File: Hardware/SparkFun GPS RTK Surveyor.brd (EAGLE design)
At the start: 68.2 x 110.1 mm, 194 parts, among them J13 Internal, J16 microSD, J17 Qwiic Right Angle, J3 USB Female Type C Connector, J4 External, J5 USB Female Type C Connector, Q1 SIL2308-TP, Q10 20V/0.2A/8MHz/1.2Ω/1Vth, Q2 MBT3904DW1T1, Q3 20V/0.2A/8MHz/1.2Ω/1Vth, Q4 20V/0.2A/8MHz/1.2Ω/1Vth, Q7 20V/0.2A/8MHz/1.2Ω/1Vth, Q9 20V/0.2A/8MHz/1.2Ω/1Vth, U1 74HC4052D, U10 MCP73833, U13 9DoF IMU, U14 1.8V/100mA, U2 AP2112K-3.3, U3 U-BLOX_ZED-F9P, U4 ADP160, U5 ESP-WROOM-32NARROW, U6 CH340C, U7 MAX17048

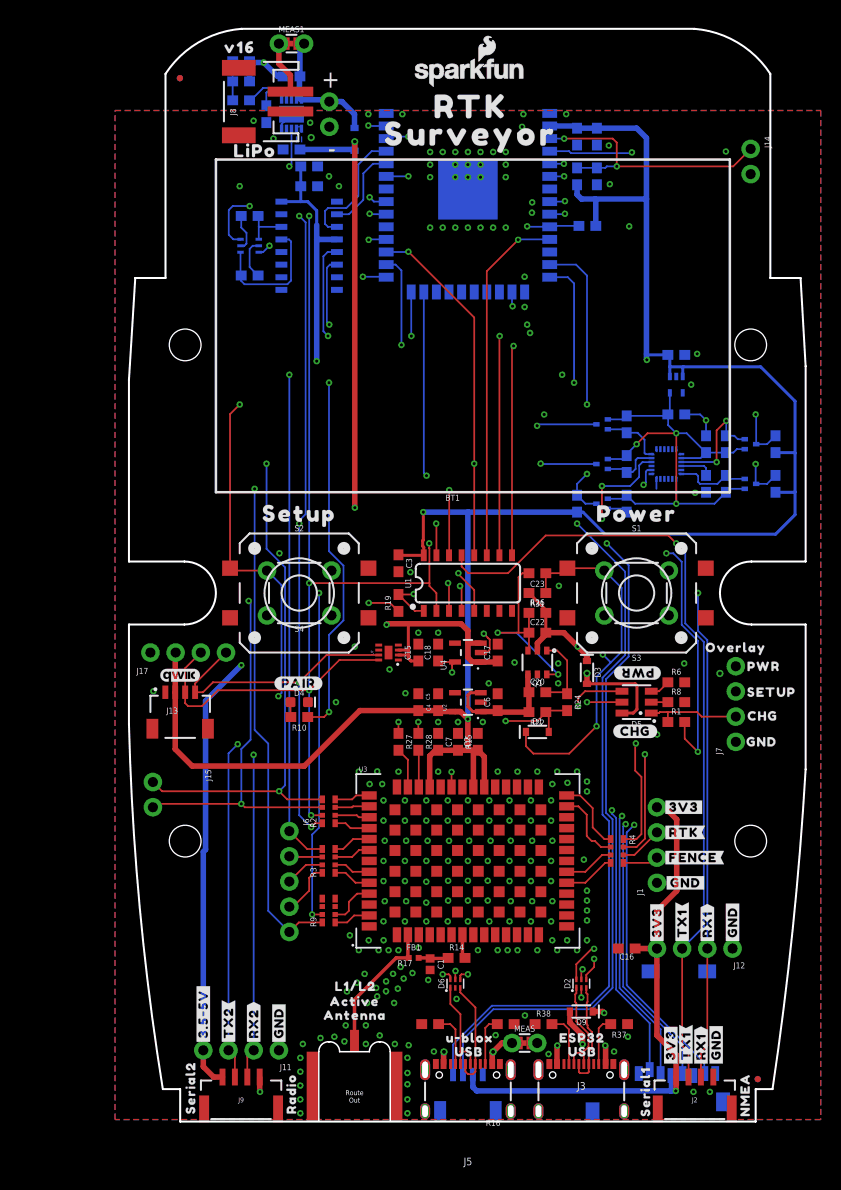
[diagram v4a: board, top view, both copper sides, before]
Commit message: Revert hardware files back to v15
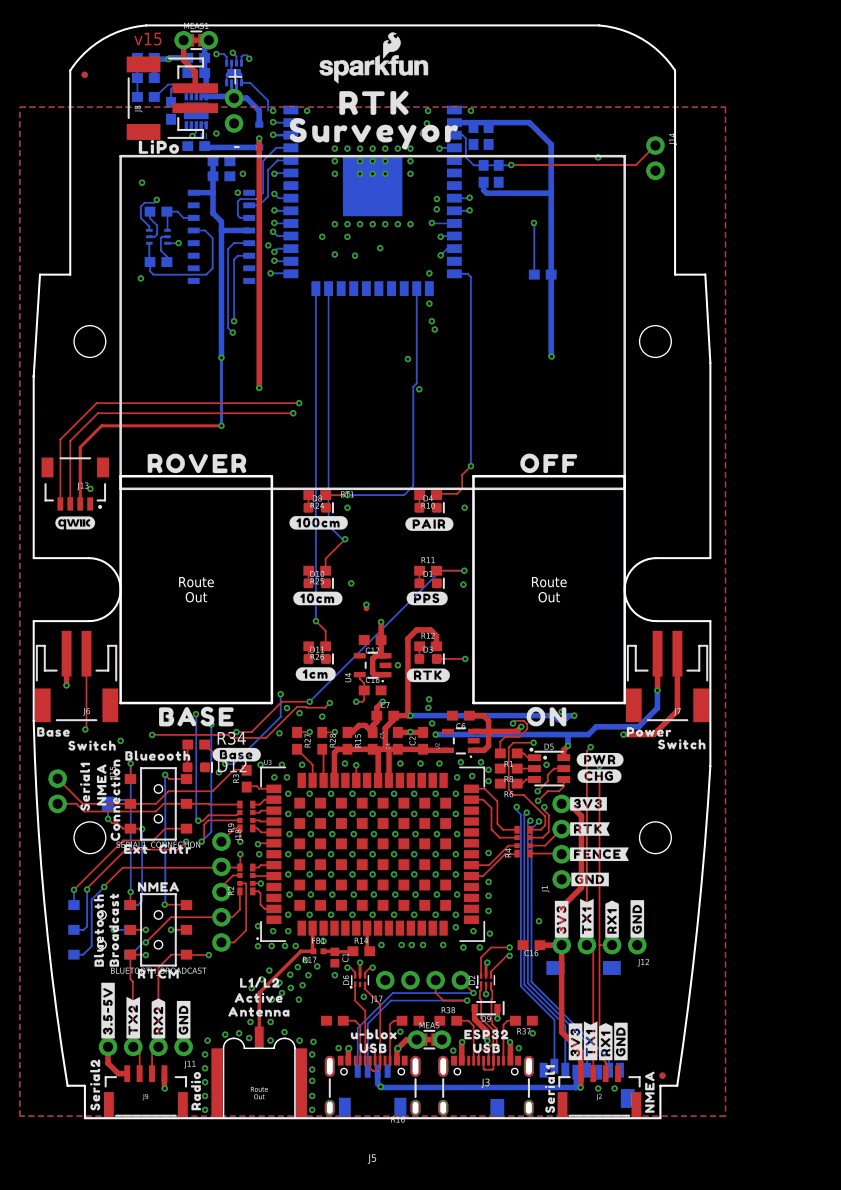
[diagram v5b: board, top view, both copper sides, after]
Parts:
- removed C20: 10uF, SparkFun-Capacitors:0603
- removed C22, C23, C3, C51, C52: 0.1uF, SparkFun-Capacitors:0603
- removed C53, C54: 1.0uF, SparkFun-Capacitors:0603
- removed Q1: SIL2308-TP, SparkFun-DiscreteSemi:SOT26
- removed Q10, Q3, Q4, Q7, Q9: 20V/0.2A/8MHz/1.2Ω/1Vth, SparkFun-DiscreteSemi:SOT-416FL
- removed R19: 1k, SparkFun-Resistors:0603
- removed R22: 100k, SparkFun-Resistors:0603
- removed R31: 10k, SparkFun-Resistors:0603
- removed R40, R41, R44, R45, R46, R47, R48: 2.2k, SparkFun-Resistors:0603
- removed R49: (no value), SparkFun-Resistors:0603
- removed S1: Power, SparkFun-Switches:TACTILE_SWITCH_PTH_6.0MM
- removed S2: Setup, SparkFun-Switches:TACTILE_SWITCH_PTH_6.0MM
- removed S3: Power, SparkFun-Switches:TACTILE_SWITCH_SMD_12MM
- removed S4: Setup, SparkFun-Switches:TACTILE_SWITCH_SMD_12MM
- removed U$95: (no value), output:AG0
- removed U$96: (no value), output:M0
- removed U1: 74HC4052D, SparkFun-IC-Logic:SO16
- removed U13: 9DoF IMU, SparkFun-Sensors:QFN24-3X3-ICM-20948
- removed U14: 1.8V/100mA, SparkFun-IC-Power:SC70
- added BLUETOOTH_BROADCAST, SERIAL1_CONNECTION, ZED_CONTROL: (no value), SparkFun-Switches:SWITCH_DPDT_SMD_AYZ0202
- added D10, D11, D8: GREEN, SparkFun-LED:LED-0603
- added D12: RED, SparkFun-LED:LED-0603
- added DUAL_OUTPUT: (no value), SparkFun-Jumpers:SMT-JUMPER_2_NO_SILK
- added J18: (no value), SparkFun-Connectors:1X05_NO_SILK
- added R11, R25: 20, SparkFun-Resistors:0603
- added R12, R34: 330, SparkFun-Resistors:0603
- added U$51: (no value), output:BROADCAST3
- added U$53: (no value), output:RTCM0
- added U$55, U$57: (no value), output:SWITCH1
- added U$56: (no value), output:POWER0
- added U$58: (no value), output:BLUEOOTH3
- added U$59: (no value), output:CNTR1
- added U$61: (no value), output:EXT0
- added U$62: (no value), output:NMEA2
- added U$63: (no value), output:SERIAL10
- added U$64: (no value), output:CONNECTION1
- added U$69, U$75, U$77, U$78: (no value), SparkFun GPS RTK Surveyor:LIGHT_PIPE_3MM
- added U$73: (no value), output:#DUAL#0
- added U$79: (no value), output:#1CM#0
- added U$80: (no value), output:#10CM#1
- added U$81: (no value), output:#100CM#2
- added U$89: (no value), output:DATA2
- added U$90: (no value), output:PORT3
- added U$91: (no value), output:PPS#RESET0
- added U$92: (no value), output:NMEA#SERIAL1
- D1: value 250mA/100V -> Yellow; device SparkFun-DiscreteSemi:SOD-323 -> SparkFun-LED:LED-0603
- D3: value 3A/10V/280mV -> WHITE; device SparkFun-DiscreteSemi:SOD-323 -> SparkFun-LED:LED-0603
- J6: value (none) -> Start Base; device SparkFun-Connectors:1X05_NO_SILK -> SparkFun-Connectors:JST-2-SMD
- J7: value (none) -> Power Switch; device SparkFun-Connectors:1X04_NO_SILK -> SparkFun-Connectors:JST-2-SMD
- R20: value 100k -> 10k
- R24: value 300k -> 20
- R26: value 100k -> 20
- R3: device SparkFun-Resistors:1206_RA -> SparkFun-Resistors:0603
- U$12: device output:X1 -> output:#RTK#0
- U$15, U$21: device output:Y2 -> SparkFun GPS RTK Surveyor:LIGHT_PIPE_3MM
- U$22: device output:X1 -> output:BASE2
- U$24: device output:SURVEYOR0 -> output:#PPS#1
- U$3: device output:#TX_RDY#0 -> SparkFun GPS RTK Surveyor:ROCKER_SWITCH
- U$31: device output:POWER0 -> output:OFF1
- U$33: device output:CHG2 -> output:#INT#0
- U$34: device output:GND3 -> SparkFun GPS RTK Surveyor:ROCKER_SWITCH
- U$4: device output:V160 -> output:#BASE#0
- U$41: device output:PWR0 -> output:BLUETOOTH2
- U$42: device output:SETUP1 -> output:ON0
- U$44: device output:OVERLAY0 -> output:ROVER3
- U$52: device output:Z0 -> output:NMEA1
- U$54: device output:Z0 -> output:BASE0
- U$9: device output:SETUP0 -> output:_SURVEYOR3
- U2: value AP2112K-3.3 -> 3.3V
- U4: value ADP160 -> 3.3V
- moved U$54 75.2 mm to (-9.14, 39.0), flipped to the top
- moved U$52 75.0 mm to (1.02, 23.4), flipped to the top
- moved U$41 73.8 mm to (-2.16, 14.6), turned to 90 degrees
- moved U$4 71.3 mm to (9.27, 36.7)
- moved U$22 64.7 mm to (2.41, 40.5), flipped to the top
- moved C15 64.0 mm to (7.62, 106.9), flipped to the bottom, turned to 0 degrees
- moved U$44 63.5 mm to (1.27, 66.0)
- moved U7 60.4 mm to (11.4, 105.4), flipped to the bottom, turned to 0 degrees
- moved U$15 58.3 mm to (7.62, 35.3), flipped to the top
- moved U$33 56.5 mm to (9.65, 27.9), flipped to the bottom
- moved U$21 52.5 mm to (19.8, 46.4), flipped to the top
- moved J17 40.6 mm to (26.7, 14.0)
- moved C10 38.1 mm to (10.2, 95.0), turned to 180 degrees
- moved U$86 36.6 mm to (34.3, 16.5), turned to 270 degrees
- moved U$70 36.4 mm to (26.7, 16.6), turned to 270 degrees
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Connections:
- net RTC_BACKUP renamed BACKUP
- removed net CHG_LED_RES: D5.CB, J7.2, R1.1
- removed net ESP_13/POWER_CTRL: D1.A, R22.1, R24.2, U5.16
- removed net ESP_14/SETUP_BUTTON: J7.3, S2.1, S4.1, U5.13
- removed net ESP_15/ICM_!CS!: Q9.3, R47.1, U5.23
- removed net ESP_18/SCK: J16.SCLK, Q3.3, U5.30
- removed net ESP_19/CIPO: J16.DO/DAT0, Q10.3, R49.1, U5.31
- removed net ESP_2/MUX_A: U1.10, U5.24
- removed net ESP_23/COPI: J16.DI/CMD, Q4.3, U5.37
- removed net ESP_26/DAC2: U1.11, U5.11
- removed net ESP_27: U5.12
- removed net ESP_4/MUX_B: U1.9, U5.26
- removed net ESP_5: U5.29
- removed net ESP_I16/ZED-TXO1: J15.1, R2.P5, U1.12, U5.27
- removed net ESP_I34/ZED_TX_READY: J6.1, R3.P5, U5.6
- removed net ESP_I36/ICM_INT: Q7.3, R45.1, U5.4
- removed net ESP_I39/ADC39: U1.4, U5.5
- removed net ESP_O17/ZED-RXI1: J15.2, R19.2, R2.P6, U1.1
- removed net EXTERNAL_DATA_IN: J12.2, J2.3, U1.3
- removed net EXTERNAL_DATA_OUT: J12.3, J2.2, U1.13
- removed net EXTINT_LV: R9.P2, U3.51
- removed net ICM-20948-LV_!CS!: Q9.2, R46.1, U13.22
- removed net ICM-20948-LV_#_1.8V: C52.1, C53.1, Q10.1, Q3.1, Q4.1, Q7.1, Q9.1, R40.2, R41.2, R44.2, R46.2, R48.2, U13.13, U13.8, U14.5
- removed net ICM-20948-LV_INT: Q7.2, R44.1, U13.12
- removed net ICM-20948-LV_SCK: Q3.2, R40.1, U13.23
- removed net ICM-20948-LV_SDI: Q4.2, R41.1, U13.24
- removed net ICM-20948-LV_SDO: Q10.2, R48.1, U13.9
- removed net N$15: C22.1, C23.2, Q1.D1, Q1.G2, R26.1
- removed net N$6: R19.1, U5.28
- removed net N$8: C20.2, Q1.G1, R24.1
- removed net POWER_BTN: C23.1, D1.C, J7.4, R31.1, S1.1, S3.1
- removed net VOUT: C20.1, C6.1, Q1.D2, R22.2, U2.1, U2.3
- removed net V_RAW: C22.2, C9.1, D3.C, D7.C, J11.4, J9.1, Q1.S2, R26.2, R31.2, U10.1, U10.2
- removed net V_USB: D2.5, D3.A, D5.AB, D6.5, D9.C, MEAS.2, MEAS.4
- removed net ZED_!RESET!: J6.3, R3.P7
- removed net ZED_!RESET!_LV: R3.P2, U3.49
- removed net ZED_EXTINT: R9.P7, U1.5
- new net 5V: C6.1, J11.4, J7.1, J9.1, U2.1, U2.3
- new net ESP_13/LED_100CM: R24.1, U5.16
- new net ESP_14: U5.13
- new net ESP_15/LED_10CM: R25.1, U5.23
- new net ESP_16/BT_RXI: BLUETOOTH_BROADCAST.2, U5.27
- new net ESP_17/BT_TXO: BLUETOOTH_BROADCAST.5, U5.28
- new net ESP_18/SD_SCK: J16.SCLK, U5.30
- new net ESP_19/SD_CIPO: J16.DO/DAT0, U5.31
- new net ESP_2/LED_1CM: R26.1, U5.24
- new net ESP_23/SD_COPI: J16.DI/CMD, U5.37
- new net ESP_26/ZED_TX_READY: J18.1, R9.P8, U5.11
- new net ESP_27/ZED_!RESET!: J18.2, R2.P5, U5.12, ZED_CONTROL.4
- new net ESP_27/ZED_!RESET!_LV: R2.P4, U3.49
- new net ESP_36/BATT_ALRT: U5.4, U7.5
- new net ESP_4/LED_BASE_STAT: R34.1, U5.26
- new net ESP_5/SWITCH_BASE_SELECT: J6.1, U5.29
- new net ESP_I34: U5.6
- new net ESP_I39: U5.5
- new net EXTERNAL_SERIAL1_RXI: SERIAL1_CONNECTION.4, ZED_CONTROL.6
- new net EXTERNAL_SERIAL1_RXI/ZED_!RESET!: J12.2, J2.3, ZED_CONTROL.5
- new net EXTERNAL_SERIAL1_TXO: DUAL_OUTPUT.2, SERIAL1_CONNECTION.1, ZED_CONTROL.3
- new net EXTERNAL_SERIAL1_TXO/PPS: J12.3, J2.2, ZED_CONTROL.2
- new net N$1: D3.A, R12.1
- new net N$17: D5.CB, R1.1
- new net N$2: D1.A, R11.1
- new net N$26: D8.A, R24.2
- new net N$27: D10.A, R25.2
- new net N$29: D11.A, R26.2
- new net NMEA-RX: BLUETOOTH_BROADCAST.6, SERIAL1_CONNECTION.6
- new net NMEA-TX: BLUETOOTH_BROADCAST.3, DUAL_OUTPUT.1, SERIAL1_CONNECTION.3
- new net VIN: C9.1, D2.5, D5.AB, D6.5, D7.C, D9.C, J7.2, MEAS.2, MEAS.4, U10.1, U10.2
- new net ZED-RXI1: J15.2, R9.P5, SERIAL1_CONNECTION.5
- new net ZED-TXO1: J15.1, R3.2, SERIAL1_CONNECTION.2
- net 3.3V: now also R12.2; no longer C3.1, C54.1, R45.2, R47.2, R49.2, U1.16, U14.1, U14.3
- net ESP_21/SDA: now also R9.P6; no longer R2.P7, U1.2
- net ESP_22/SCL: now also R9.P7; no longer R2.P8, U1.15
- net ESP_26/ZED_TX_READY_LV: now also R9.P1; no longer R3.P4
- net FENCE_LV: now also R4.P8; no longer R4.P4
- net GND: now also D1.C, D10.C, D11.C, D12.C, D8.C, J6.2; no longer C3.2, C51.2, C52.2, C53.2, C54.2, J7.1, Q1.S1, S1.3, S2.3, S3.3, S4.3, U1.6, U1.7, U1.8, U13.18, U13.20, U14.2
- net N$30: now also D12.A, R34.2; no longer C51.1, U13.10
- net PPS: now also R2.P1; no longer R9.P1
- net RTK_LV: now also R4.P7; no longer R4.P3
- net RX2_LV: now also R4.P6; no longer R4.P2
- net RXLV: now also R9.P4; no longer R2.P3
- net SCL_LV: now also R9.P2; no longer R2.P1
- net SDA_LV: now also R9.P3; no longer R2.P2
- net TX2_LV: now also R4.P5; no longer R4.P1
- net TXLV: now also R3.1; no longer R2.P4
- net ZED-RXI2: now also BLUETOOTH_BROADCAST.4, R4.P3; no longer R4.P7
- net ZED-TXO2: now also BLUETOOTH_BROADCAST.1, R4.P4; no longer R4.P8
- net ZED_!SAFE!: now also J18.3, R2.P6; no longer J6.4, R3.P8
- net ZED_!SAFE!_LV: now also R2.P3; no longer R3.P1
- net ZED_D_SEL: now also J18.5, R2.P7; no longer J6.2, R3.P6
- net ZED_D_SEL_LV: now also R2.P2; no longer R3.P3
- net ZED_FENCE_STAT: now also R4.P1; no longer R4.P5
- net ZED_PPS_STAT: now also J18.4, R11.2, R2.P8, ZED_CONTROL.1; no longer J6.5, R9.P8, U1.14
- net ZED_RTK_STAT: now also D3.C, R4.P2; no longer R4.P6
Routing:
- net VIN: track 0.00 -> 189.6 mm, vias 0 -> 9
- net V_RAW: track 149.4 -> 0.00 mm, vias 5 -> 0
- net ESP_19/CIPO: track 143.0 -> 0.00 mm, vias 5 -> 0
- net ESP_14/SETUP_BUTTON: track 133.0 -> 0.00 mm, vias 3 -> 0
- net ESP_23/COPI: track 127.2 -> 0.00 mm, vias 4 -> 0
- net ESP_23/SD_COPI: track 0.00 -> 120.9 mm, vias 0 -> 3
- net ESP_18/SCK: track 120.2 -> 0.00 mm, vias 4 -> 0
- net ESP_19/SD_CIPO: track 0.00 -> 115.8 mm, vias 0 -> 3
- net ESP_18/SD_SCK: track 0.00 -> 113.2 mm, vias 0 -> 3
- net 5V: track 0.00 -> 112.3 mm, vias 0 -> 2
- net ESP_I16/ZED-TXO1: track 108.4 -> 0.00 mm, vias 4 -> 0
- net ESP_27/ZED_!RESET!: track 0.00 -> 102.6 mm, vias 0 -> 4
- net EXTERNAL_SERIAL1_TXO/PPS: track 0.00 -> 101.6 mm, vias 0 -> 2
- net ESP_I34/ZED_TX_READY: track 100.1 -> 0.00 mm, vias 3 -> 0
- net EXTERNAL_SERIAL1_RXI/ZED_!RESET!: track 0.00 -> 99.7 mm, vias 0 -> 3
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- added copper zone on layer 16, net VIN
- removed copper zone on layer 16, net V_RAW
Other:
- outline, holes or cut-outs redrawn
- board text added: "-ND"
- board text added: "10.16mm / 0.4" is common"
- board text added: "12.7mm / 0.5" is common"
- board text added: "12x12mm switch height: 8.5mm"
- board text added: "350-3725-ND (Flat $0.25)"
- board text added: "350-3726-ND (Flat $0.25)"
- board text added: "350-3738-ND (Dome $0.25)"
- board text added: "Gap to base switch: 3.4mm"
- board text added: "Inside height: 18.5mm"
- board text added: "LED Height: 0.8mm"
- board text added: "NA"
- board text added: "Pipe length: 12.08-12.85mm"
- board text added: "Recommended air gap: 0.5-1.27mm"
- board text added: "Rocker height: 16.7mm"
- board text added: "Route Out"
- board text added: "Thckness of top cover: 2.25mm"
- board text added: "Top Cover thickness: 2.25mm"
- board text added: "Top PCB surface to inside lid: 11.9mm"
- board text added: "v15"
- board text removed: "11.9+2.75=14.65mm"
- board text removed: "11.9-3.4=8.5mm actuator length on square button"
- board text removed: "11.9-8=3.9"
- board text removed: "18.5-5-1.6=11.9mm"
- board text removed: "Distance from PCB surface to outer surface of lid:"
- board text removed: "Distance from inner lid to PCB surface:"

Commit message: v16 hardware: Change out EOL'd LED. Add ESD to RF path.
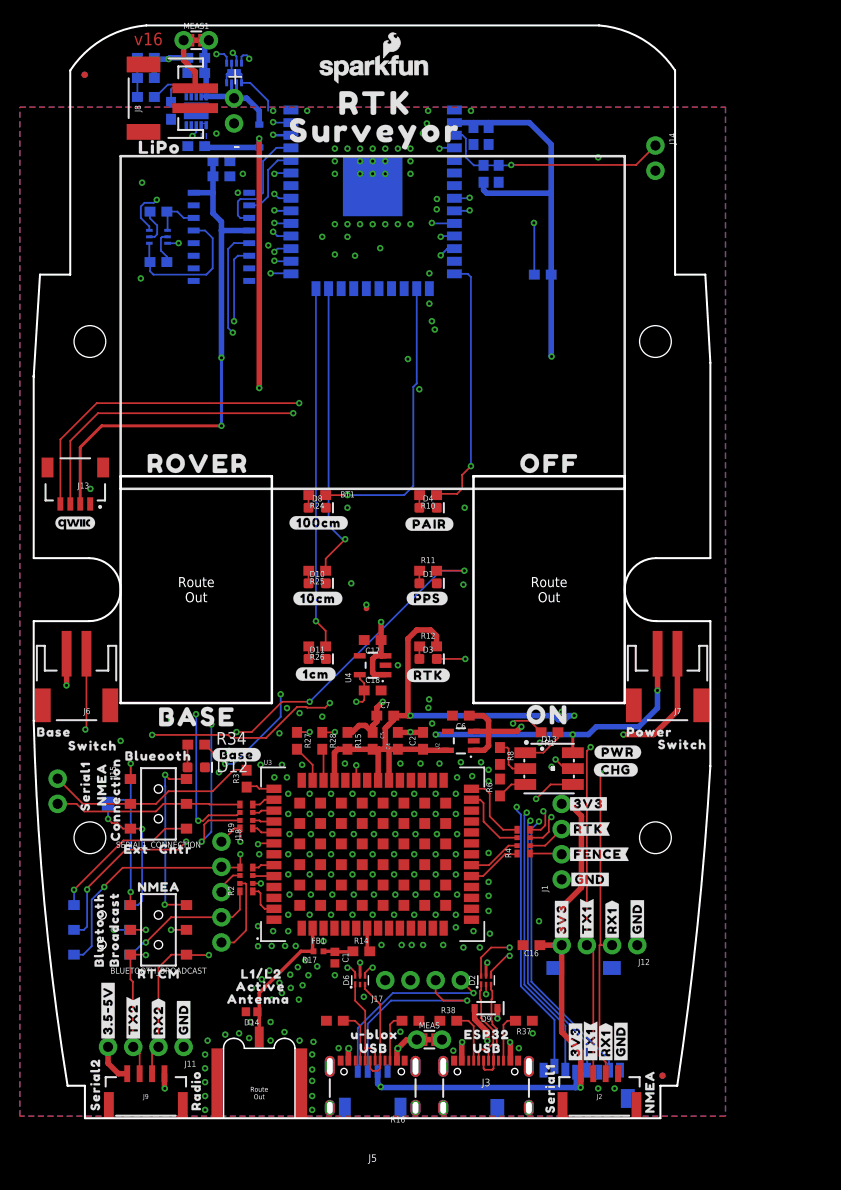
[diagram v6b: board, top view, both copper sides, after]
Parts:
- removed D5: RGB, SparkFun-LED:PLCC-6-LED
- added D13: (no value), SparkFun-LED:LED-TRICOLOR-5050
- added D14: PESD0402, SparkFun-DiscreteSemi:0402
- moved R1 4.63 mm to (43.2, 39.0)
- moved U$25 1.93 mm to (47.8, 37.0)
- moved U$8 1.77 mm to (49.9, 35.2)
- moved R8 1.55 mm to (38.2, 36.6), turned to 270 degrees
- moved U$6 1.29 mm to (10.0, 12.1)
- moved U$18 1.17 mm to (10.9, 13.3)
- moved R6 0.97 mm to (38.2, 33.4), turned to 90 degrees
- moved U$19 0.91 mm to (11.4, 14.6)
- moved U$42 0.20 mm to (39.5, 40.7)
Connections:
- removed net N$10: D5.CG, R6.1
- removed net N$14: D5.CR, R8.1
- removed net N$17: D5.CB, R1.1
- new net N$6: D13.1, R1.1
- new net N$7: D13.3, R6.1
- new net N$8: D13.2, R8.1
- net ESP_32/PWR_LVL_RED: now also D13.5; no longer D5.AR
- net ESP_33/PWR_LVL_GRN: now also D13.4; no longer D5.AG
- net GND: now also D14.2
- net GPS_ANT1: now also D14.1
- net VIN: now also D13.6; no longer D5.AB
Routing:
- net N$6: track 0.00 -> 4.50 mm
- net N$8: track 0.00 -> 4.37 mm
- net ZED-TXO2: track 93.2 -> 89.7 mm, vias 3 -> 4
- net CHG_LED: track 100.1 -> 96.9 mm
- net ZED_RTK_STAT: track 34.2 -> 37.3 mm
- net N$7: track 0.00 -> 3.03 mm
- net ESP_32/PWR_LVL_RED: track 71.6 -> 69.1 mm
- net N$10: track 1.91 -> 0.00 mm
- net N$17: track 1.91 -> 0.00 mm
- net N$14: track 1.74 -> 0.00 mm
- net EXTERNAL_SERIAL1_RXI/ZED_!RESET!: track 99.7 -> 99.0 mm
- net VIN: track 189.6 -> 189.0 mm
- net TX2_LV: track 7.66 -> 8.32 mm
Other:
- board text added: "v16"
- board text removed: "v15"

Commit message: Update panel files to v1.6 PCB
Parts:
- removed U5: ESP-WROOM-32NARROW, SparkFun-RF:ESP-WROOM-32-NARROW
- added U1: ESP-WROOM-3232D-NARROW, SparkFun-RF:ESP-WROOM-32D-NARROW
- BT1: value LIPO-OUTLINE1100 -> LIPO-OUTLINE1000
- moved BT1 30.6 mm to (25.4, 80.6)
- moved R6 0.10 mm to (38.2, 33.3)
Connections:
- net 3.3V: now also U1.2; no longer U5.2
- net ESP32_EN: now also U1.3; no longer U5.3
- net ESP32_RXI: now also U1.34; no longer U5.34
- net ESP32_TXO: now also U1.35; no longer U5.35
- net ESP_0/BOOT: now also U1.25; no longer U5.25
- net ESP_12/LED_BLUETOOTH: now also U1.14; no longer U5.14
- net ESP_13/LED_100CM: now also U1.16; no longer U5.16
- net ESP_14: now also U1.13; no longer U5.13
- net ESP_15/LED_10CM: now also U1.23; no longer U5.23
- net ESP_16/BT_RXI: now also U1.27; no longer U5.27
- net ESP_17/BT_TXO: now also U1.28; no longer U5.28
- net ESP_18/SD_SCK: now also U1.30; no longer U5.30
- net ESP_19/SD_CIPO: now also U1.31; no longer U5.31
- net ESP_2/LED_1CM: now also U1.24; no longer U5.24
- net ESP_21/SDA: now also U1.33; no longer U5.33
- net ESP_22/SCL: now also U1.36; no longer U5.36
- net ESP_23/SD_COPI: now also U1.37; no longer U5.37
- net ESP_25/SD_!CS!: now also U1.10; no longer U5.10
- net ESP_26/ZED_TX_READY: now also U1.11; no longer U5.11
- net ESP_27/ZED_!RESET!: now also U1.12; no longer U5.12
- net ESP_32/PWR_LVL_RED: now also U1.8; no longer U5.8
- net ESP_33/PWR_LVL_GRN: now also U1.9; no longer U5.9
- net ESP_36/BATT_ALRT: now also U1.4; no longer U5.4
- net ESP_4/LED_BASE_STAT: now also U1.26; no longer U5.26
- net ESP_5/SWITCH_BASE_SELECT: now also U1.29; no longer U5.29
- net ESP_I34: now also U1.6; no longer U5.6
- net ESP_I35: now also U1.7; no longer U5.7
- net ESP_I39: now also U1.5; no longer U5.5
- net GND: now also U1.1, U1.15, U1.38, U1.GND1, U1.GNDT1, U1.GNDT2, U1.GNDT3, U1.GNDT4, U1.GNDT5, U1.GNDT6, U1.GNDT7, U1.GNDT8; no longer U5.1, U5.15, U5.38, U5.GND
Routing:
- net TX2_LV: track 8.32 -> 7.67 mm
